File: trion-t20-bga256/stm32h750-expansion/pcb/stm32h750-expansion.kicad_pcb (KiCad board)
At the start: 4 copper layers, 48 x 45.5 mm, 77 parts, among them J1 CONN_02x18, J2 CORTEX_DEBUG_ETM, J3 U.FL, J4 U.FL, J5 U.FL, J6 CONN_01X03, J7 CONN_01X03, J8 PMOD_HOST, M1 MECHANICAL, U1 STM32H750XBH6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

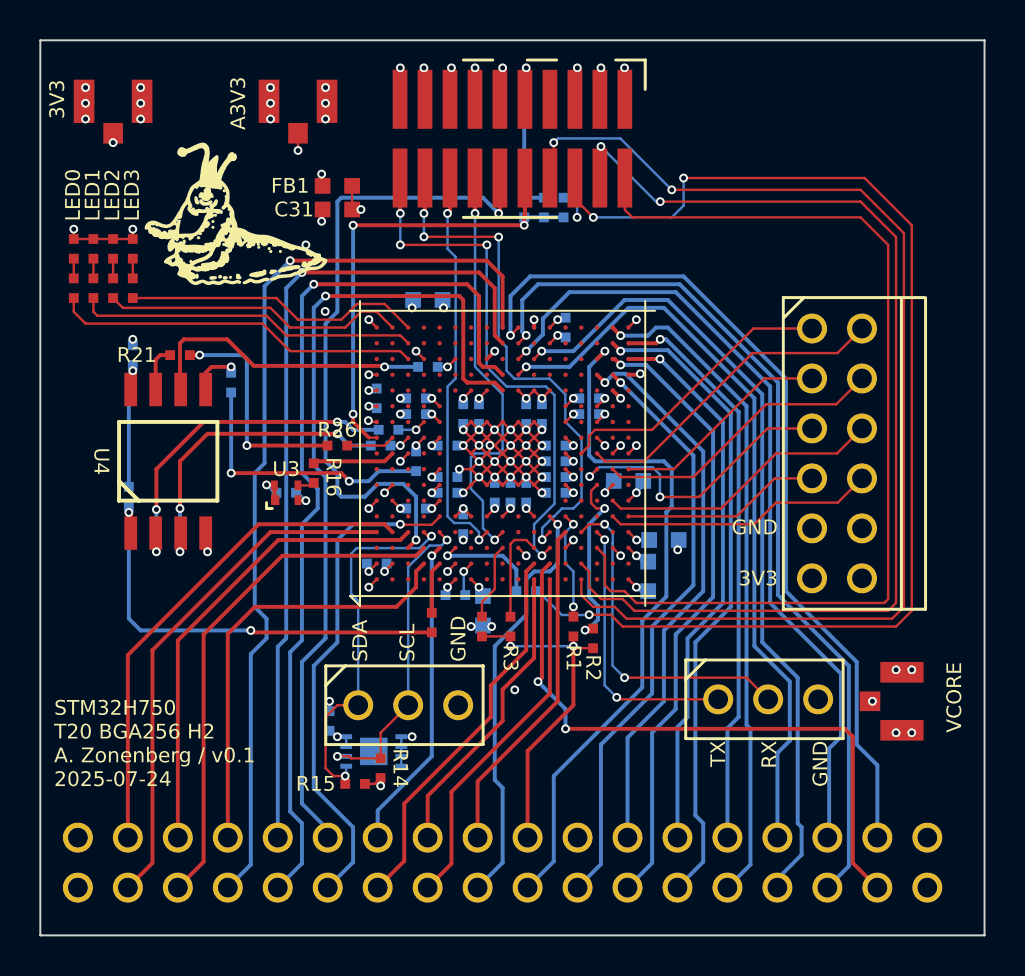
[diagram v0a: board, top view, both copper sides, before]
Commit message: Finished zone fill tweaks, ready to order
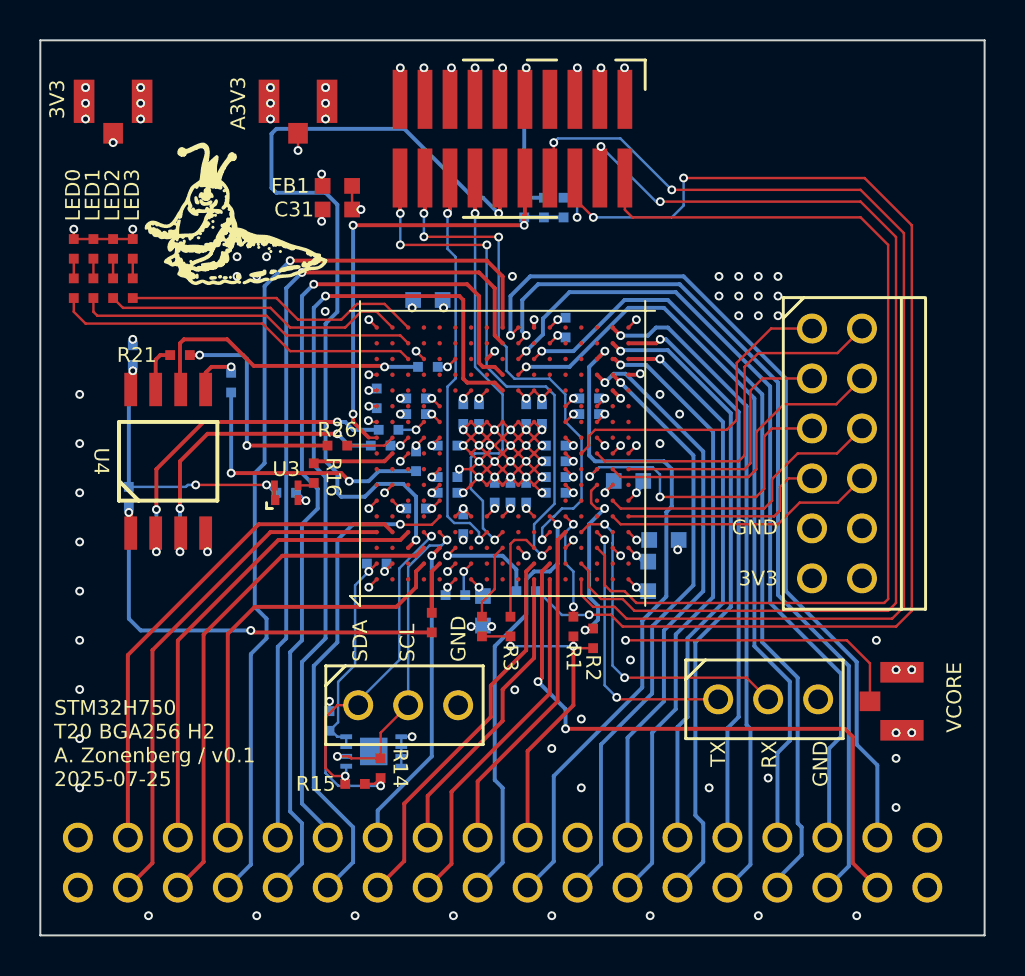
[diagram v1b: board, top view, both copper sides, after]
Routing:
- net /3V3: track 206.9 -> 228.0 mm
- net /TRACECLK: track 33.1 -> 44.2 mm
- net /PMOD_DQ4: track 16.4 -> 19.1 mm
- net /I2C_SDA: track 19.0 -> 16.8 mm
- net /PMOD_DQ1: track 11.2 -> 13.4 mm
- net /PMOD_DQ0: track 14.7 -> 16.4 mm
- net /PMOD_DQ2: track 14.8 -> 16.3 mm
- net /VCORE: track 47.9 -> 49.0 mm
- net /PMOD_DQ5: track 14.9 -> 16.0 mm
- net /PMOD_DQ3: track 10.1 -> 10.8 mm
- net /PMOD_DQ6: track 14.5 -> 15.2 mm
- net /GND: track 345.3 -> 344.7 mm, vias 92 -> 136
- added copper zone on In2.Cu, net /3V3
- added copper zone on In2.Cu, net /A3V3
- added copper zone on In1.Cu, net /GND
- added copper zone on In2.Cu, net /GND
- added copper zone on In2.Cu, net /VCORE
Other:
- board text added: "STM32H750 T20 BGA256 H2 A. Zonenberg / v0.1 2025-07-25"
- board text removed: "STM32H750 T20 BGA256 H2 A. Zonenberg / v0.1 2025-07-24"

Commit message: Updated final version of stm32h750-expansion with routing tweaks and export config
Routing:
- net /FMC_AD11: track 44.4 -> 45.2 mm
- net /FMC_AD9: track 41.2 -> 41.9 mm
- net /FMC_AD10: track 45.5 -> 46.2 mm
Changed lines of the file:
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@@
 			(outputformat 1)
 			(mirror no)
-			(drillshape 1)
+			(drillshape 0)
 			(scaleselection 1)
-			(outputdirectory "")
+			(outputdirectory "output/")
 		)
 	)
@@
 	)
 	(segment
-		(start 67.6 44.6)
-		(end 67.6 55.6)
+		(start 67.6 57.4)
+		(end 69 58.8)
 		(width 0.2)
 		(layer "B.Cu")
@@
 	)
 	(segment
-		(start 57.4 39.8)
-		(end 62.8 39.8)
+		(start 55.2 42.8)
+		(end 56.05 41.95)
 		(width 0.2)
 		(layer "B.Cu")
@@
 	)
 	(segment
-		(start 56.05 41.95)
-		(end 56.05 41.15)
+		(start 71.2 62.4)
+		(end 70.6 63)
 		(width 0.2)
 		(layer "B.Cu")
@@
 	)
 	(segment
-		(start 67.6 55.6)
-		(end 71.2 59.2)
+		(start 62.8 39.8)
+		(end 67.6 44.6)
 		(width 0.2)
 		(layer "B.Cu")
@@
 	)
 	(segment
-		(start 62.8 39.8)
-		(end 67.6 44.6)
+		(start 69 58.8)
+		(end 70.2 58.8)
 		(width 0.2)
 		(layer "B.Cu")
@@
 	)
 	(segment
-		(start 71.2 59.2)
-		(end 71.2 62.4)
+		(start 67.6 44.6)
+		(end 67.6 57.4)
 		(width 0.2)
 		(layer "B.Cu")
@@
 	)
 	(segment
-		(start 56.05 41.15)
-		(end 57.4 39.8)
+		(start 70.2 58.8)
+		(end 71.2 59.8)
 		(width 0.2)
 		(layer "B.Cu")
@@
 	)
 	(segment
-		(start 55.2 42.8)
-		(end 56.05 41.95)
+		(start 56.05 41.95)
+		(end 56.05 41.15)
 		(width 0.2)
 		(layer "B.Cu")
@@
 	)
 	(segment
-		(start 71.2 62.4)
-		(end 70.6 63)
+		(start 71.2 59.8)
+		(end 71.2 62.4)
+		(width 0.2)
+		(layer "B.Cu")
+		(net 26)
+	)
+	(segment
+		(start 56.05 41.15)
+		(end 57.4 39.8)
+		(width 0.2)
+		(layer "B.Cu")
+		(net 26)
+	)
+	(segment
+		(start 57.4 39.8)
+		(end 62.8 39.8)
 		(width 0.2)
 		(layer "B.Cu")
@@
 	)
 	(segment
-		(start 68.4 44.2)
-		(end 63.2 39)
+		(start 54.4 40)
+		(end 54.4 42)
 		(width 0.2)
 		(layer "B.Cu")
@@
 	)
 	(segment
-		(start 68.4 55)
+		(start 55.4 39)
+		(end 54.4 40)
+		(width 0.2)
+		(layer "B.Cu")
+		(net 31)
+	)
+	(segment
+		(start 68.4 57)
 		(end 68.4 44.2)
 		(width 0.2)
@@
 	)
 	(segment
-		(start 72 58.6)
-		(end 68.4 55)
+		(start 69.4 58)
+		(end 68.4 57)
 		(width 0.2)
 		(layer "B.Cu")
@@
 	)
 	(segment
-		(start 54.4 40)
-		(end 54.4 42)
+		(start 73.05 67.53)
+		(end 73.05 63.85)
 		(width 0.2)
 		(layer "B.Cu")
@@
 	)
 	(segment
-		(start 55.4 39)
-		(end 54.4 40)
+		(start 72 62.8)
+		(end 72 59.2)
 		(width 0.2)
 		(layer "B.Cu")
@@
 	)
 	(segment
-		(start 73.05 67.53)
-		(end 73.05 63.85)
+		(start 70.8 58)
+		(end 69.4 58)
 		(width 0.2)
 		(layer "B.Cu")
@@
 	)
 	(segment
-		(start 63.2 39)
-		(end 55.4 39)
+		(start 72 59.2)
+		(end 70.8 58)
 		(width 0.2)
 		(layer "B.Cu")
@@
 	)
 	(segment
-		(start 72 62.8)
-		(end 72 58.6)
+		(start 68.4 44.2)
+		(end 63.2 39)
+		(width 0.2)
+		(layer "B.Cu")
+		(net 31)
+	)
+	(segment
+		(start 63.2 39)
+		(end 55.4 39)
 		(width 0.2)
 		(layer "B.Cu")
@@
 	)
 	(segment
-		(start 55 41.8)
-		(end 55 40.2)
+		(start 55.2 42)
+		(end 55 41.8)
 		(width 0.2)
 		(layer "B.Cu")
@@
 	)
 	(segment
-		(start 68 55.2)
-		(end 71.6 58.8)
+		(start 55 40.2)
+		(end 55.8 39.4)
 		(width 0.2)
 		(layer "B.Cu")
@@
 	)
 	(segment
-		(start 63 39.4)
-		(end 68 44.4)
+		(start 71.6 68.980001)
+		(end 70.51 70.070001)
 		(width 0.2)
 		(layer "B.Cu")
@@
 	)
 	(segment
-		(start 55 40.2)
-		(end 55.8 39.4)
+		(start 68 57.2)
+		(end 69.2 58.4)
 		(width 0.2)
 		(layer "B.Cu")
@@
 	)
 	(segment
-		(start 71.6 68.980001)
-		(end 70.51 70.070001)
+		(start 68 44.4)
+		(end 68 57.2)
 		(width 0.2)
 		(layer "B.Cu")
@@
 	)
 	(segment
-		(start 55.8 39.4)
-		(end 63 39.4)
+		(start 69.2 58.4)
+		(end 70.4 58.4)
 		(width 0.2)
 		(layer "B.Cu")
@@
 	)
 	(segment
-		(start 71.6 58.8)
-		(end 71.6 68.980001)
+		(start 55 41.8)
+		(end 55 40.2)
 		(width 0.2)
 		(layer "B.Cu")
@@
 	)
 	(segment
-		(start 68 44.4)
-		(end 68 55.2)
+		(start 63 39.4)
+		(end 68 44.4)
 		(width 0.2)
 		(layer "B.Cu")
@@
 	)
 	(segment
-		(start 55.2 42)
-		(end 55 41.8)
+		(start 55.8 39.4)
+		(end 63 39.4)
+		(width 0.2)
+		(layer "B.Cu")
+		(net 37)
+	)
+	(segment
+		(start 70.4 58.4)
+		(end 71.6 59.6)
+		(width 0.2)
+		(layer "B.Cu")
+		(net 37)
+	)
+	(segment
+		(start 71.6 59.6)
+		(end 71.6 68.980001)
 		(width 0.2)
 		(layer "B.Cu")

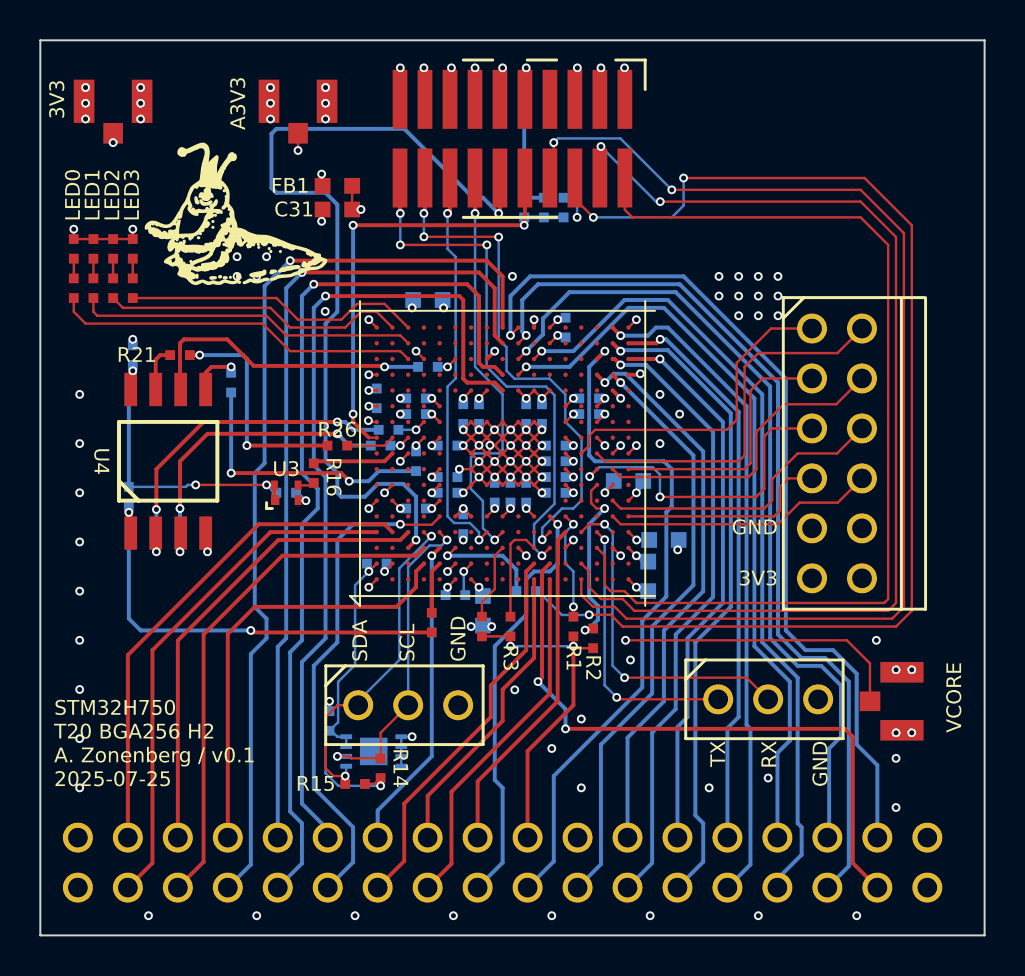
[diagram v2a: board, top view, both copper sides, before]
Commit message: Updated stm32h750-expansion for v0.2
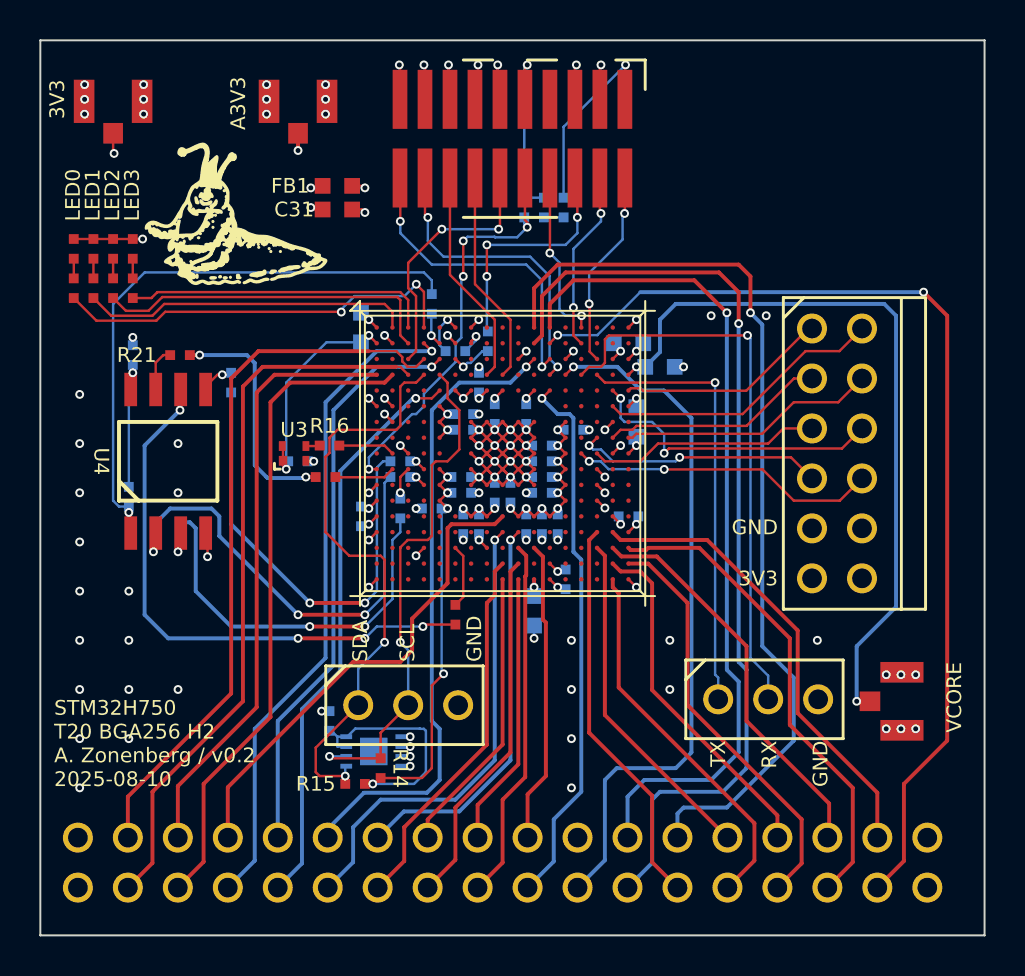
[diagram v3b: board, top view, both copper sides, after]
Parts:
- removed R2, R4: DNP, azonenberg_pcb:EIA_0402_RES_NOSILK
- removed R23: 33, azonenberg_pcb:EIA_0402_RES_NOSILK
- removed R3: 0, azonenberg_pcb:EIA_0402_RES_NOSILK
- R1: value DNP -> 33
- R24: moved to B.Cu
- moved R24 16.2 mm to (50.4, 40.4), turned to -90 degrees
- moved R5 12.8 mm to (53.2, 42.3), turned to -90 degrees
- moved R6 12.4 mm to (51.6, 42.8)
- moved C7 11.9 mm to (60.4, 42.4), turned to 180 degrees
- moved C29 11.4 mm to (50.4, 50.8), turned to 180 degrees
- moved C30 9.63 mm to (57.2, 54.4), turned to 90 degrees
- moved C6 8.80 mm to (62.0, 43.6)
- moved C23 8.50 mm to (55.2, 51.6), turned to -90 degrees
- moved C28 8.50 mm to (52.0, 51.6), turned to -90 degrees
- moved C26 7.38 mm to (55.2, 46.0), turned to -90 degrees
- moved C10 6.88 mm to (56.8, 51.6)
- moved C25 6.32 mm to (60.4, 51.2), turned to 180 degrees
- moved C32 6.05 mm to (46.8, 51.2), turned to -90 degrees
- moved R1 6.03 mm to (51.6, 56.2)
- moved R7 5.66 mm to (52.8, 44.4)
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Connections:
- J1 pad 10: /FMC_AD14 -> /FMC_A16
- J1 pad 11: /FMC_AD15 -> /FMC_AD1
- J1 pad 12: /FMC_A18 -> /FMC_NWE
- J1 pad 13: /FMC_A17 -> /FMC_NWAIT
- J1 pad 14: /FMC_AD1 -> /FMC_NOE
- J1 pad 15: /FMC_AD0 -> /FMC_AD2
- J1 pad 17: /FMC_A16 -> /FMC_AD3
- J1 pad 18: /FMC_CS_N -> /FMC_AD12
- J1 pad 19: /FMC_AD3 -> /FMC_AD9
- J1 pad 20: /FMC_AD2 -> /FMC_AD11
- J1 pad 21: /FMC_NOE -> /FMC_AD10
- J1 pad 22: /FMC_NWE -> /FMC_AD4
- J1 pad 23: /FMC_NWAIT -> /FMC_AD5
- J1 pad 24: /FMC_NL -> /FMC_AD8
- J1 pad 25: /FMC_A22 -> /FMC_AD6
- J1 pad 26: /FMC_AD7 -> /FMC_CS_N
- J1 pad 27: /FMC_AD6 -> /FMC_A22
- J1 pad 28: /FMC_AD5 -> /FMC_NL
- J1 pad 29: /FMC_AD4 -> /FMC_NBL1
- J1 pad 30: /FMC_NBL1 -> /FMC_AD7
- J1 pad 31: /FMC_NBL0 -> /FMC_A20
- J1 pad 32: /FMC_A19 -> /FMC_A21
- J1 pad 33: /FMC_A21 -> /FMC_A19
- J1 pad 34: /FMC_A20 -> /FMC_NBL0
- J1 pad 4: /FMC_AD11 -> /FMC_AD0
- J1 pad 5: /FMC_AD10 -> /FMC_A18
- J1 pad 6: /FMC_AD9 -> /FMC_A17
- J1 pad 7: /FMC_AD12 -> /FMC_AD14
- J1 pad 8: /FMC_AD8 -> /FMC_AD15
- R1 pad 1: /FMC_CS_N -> /QSPI_SCK
- R1 pad 2: Net-(U1C-PC8) -> Net-(U1B-PB2)
- U1 pad A2: unconnected-(U1I-PI6-PadA2) -> /MCU_LED1
- U1 pad A3: unconnected-(U1I-PI5-PadA3) -> /MCU_LED3
- U1 pad A4: unconnected-(U1I-PI4-PadA4) -> /MCU_LED0
- U1 pad B3: unconnected-(U1I-PI7-PadB3) -> /MCU_LED2
- U1 pad C11: Net-(U1D-PD7) -> /FMC_CS_N
- U1 pad C9: Net-(U1G-PG12) -> unconnected-(U1G-PG12-PadC9)
- U1 pad E13: Net-(U1C-PC8) -> unconnected-(U1C-PC8-PadE13)
- U1 pad E16: /PMOD_DQ7 -> /PMOD_DQ6
- U1 pad E17: /PMOD_DQ3 -> /PMOD_DQ0
- U1 pad F16: /PMOD_DQ6 -> /PMOD_DQ4
- U1 pad G15: Net-(U1G-PG6) -> unconnected-(U1G-PG6-PadG15)
- U1 pad H15: /PMOD_DQ2 -> /PMOD_DQ3
- U1 pad H16: /PMOD_DQ5 -> /PMOD_DQ1
- U1 pad H17: /PMOD_DQ1 -> /PMOD_DQ5
- U1 pad J14: /PMOD_DQ0 -> /PMOD_DQ7
- U1 pad J15: /PMOD_DQ4 -> /PMOD_DQ2
- U1 pad R3: /MCU_LED0 -> unconnected-(U1A-PA6-PadR3)
- U1 pad T3: /MCU_LED1 -> unconnected-(U1A-PA5-PadT3)
- U1 pad U2: /MCU_LED2 -> unconnected-(U1A-PA3-PadU2)
- U1 pad U3: /MCU_LED3 -> unconnected-(U1A-PA4-PadU3)
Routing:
- net /GND: track 344.7 -> 290.9 mm, vias 136 -> 114
- net /JTAG_TDI: track 58.4 -> 8.75 mm
- net /JTAG_TDO: track 59.8 -> 11.9 mm
- net /JTAG_TCK: track 53.1 -> 9.17 mm
- net /JTAG_TMS: track 50.7 -> 10.1 mm, vias 0 -> 2
- net /FMC_AD4: track 47.4 -> 14.7 mm, vias 1 -> 0
- net /FMC_NWE: track 15.4 -> 46.9 mm, vias 0 -> 1
- net /FMC_AD11: track 45.2 -> 14.0 mm, vias 1 -> 0
- net /TRACECLK: track 44.2 -> 13.2 mm
- net /FMC_NWAIT: track 19.8 -> 48.3 mm, vias 0 -> 1
- net /FMC_AD10: track 46.2 -> 18.4 mm, vias 1 -> 0
- net /FMC_AD12: track 40.8 -> 15.4 mm, vias 1 -> 0
- net /FMC_NOE: track 18.2 -> 42.6 mm, vias 0 -> 1
- net /FMC_AD9: track 41.9 -> 18.5 mm, vias 1 -> 0
- net /FMC_AD5: track 42.3 -> 19.1 mm, vias 1 -> 0
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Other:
- board text added: "STM32H750 T20 BGA256 H2 A. Zonenberg / v0.2 2025-08-10"
- board text removed: "STM32H750 T20 BGA256 H2 A. Zonenberg / v0.1 2025-07-25"
